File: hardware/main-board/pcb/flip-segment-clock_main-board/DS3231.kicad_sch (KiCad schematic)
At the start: 1 part, among them IC1 DS3231MZ+TRL

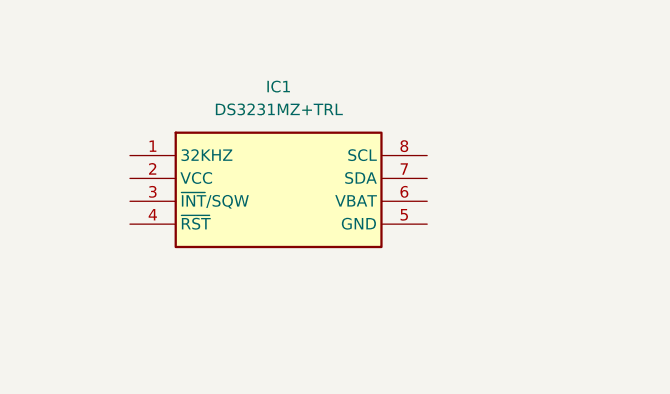
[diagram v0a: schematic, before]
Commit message: Refining design of the segment drivers
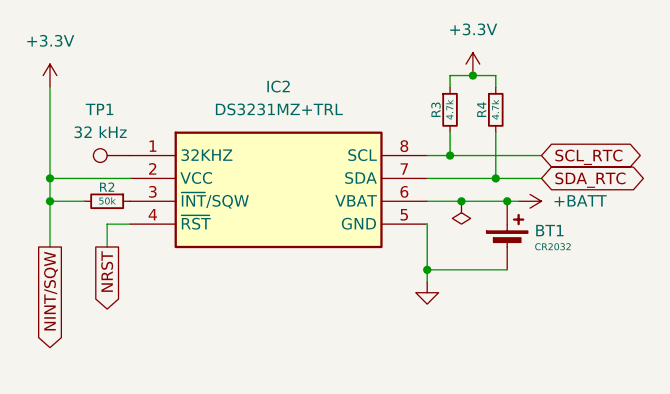
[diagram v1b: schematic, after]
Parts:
- added BT1: CR2032, Battery:BatteryHolder_Keystone_1057_1x2032, symbol Device:Battery_Cell
- added R2: 50k, Resistor_SMD:R_0402_1005Metric, symbol Device:R_Small
- added R3, R4: 4.7k, Resistor_SMD:R_0402_1005Metric, symbol Device:R_Small
- added TP1: 32 kHz, TestPoint:TestPoint_Pad_D2.5mm, symbol Connector:TestPoint
- IC2: renamed from IC1; footprint SOIC127P600X175-8N -> SamacSys_Parts:SOIC127P600X175-8N
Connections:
- net at IC2.1 (32KHZ): now also TP1.1
- net +3.3V: now reaches IC2.2 (VCC)
- net +3.3V: now also R2.2, R3.1, R4.1
- net at IC2.3 (~{INT}/SQW): now also R2.1
- net NRST: now reaches IC2.4 (~{RST})
- net GND: now reaches IC2.5 (GND)
- net GND: now also BT1.2 (-)
- net +BATT: now reaches IC2.6 (VBAT)
- net +BATT: now also BT1.1 (+)
- net SDA_RTC: now reaches IC2.7 (SDA)
- net SDA_RTC: now also R4.2
- net SCL_RTC: now reaches IC2.8 (SCL)
- net SCL_RTC: now also R3.2

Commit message: Unsure
Unsure of previous changes due to time off. Currently edited the lessons learned page.
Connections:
- net SCL_RTC renamed SCL
- net SDA_RTC renamed SDA
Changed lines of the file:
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@@
 		)
 	)
-	(global_label "SCL_RTC"
+	(global_label "SCL"
 		(shape bidirectional)
 		(at 102.87 58.42 0)
@@
 		)
 		(property "Intersheetrefs" "${INTERSHEET_REFS}"
-			(at 114.9493 58.42 0)
+			(at 110.4741 58.42 0)
 			(effects
 				(font
@@
 		)
 	)
-	(global_label "SDA_RTC"
+	(global_label "SDA"
 		(shape bidirectional)
 		(at 102.87 60.96 0)
@@
 		)
 		(property "Intersheetrefs" "${INTERSHEET_REFS}"
-			(at 115.0098 60.96 0)
+			(at 110.5346 60.96 0)
 			(effects
 				(font
